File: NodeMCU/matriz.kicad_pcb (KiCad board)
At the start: 2 copper layers, 69 x 68 mm, 25 parts, among them J1 Conn_01x05, Q1 Q_NPN_CBE, Q2 Q_NPN_CBE, Q3 Q_NPN_CBE, SW1 SW_Push_Open, SW2 SW_Push, U3 NodeMCU1.0(ESP-12E)

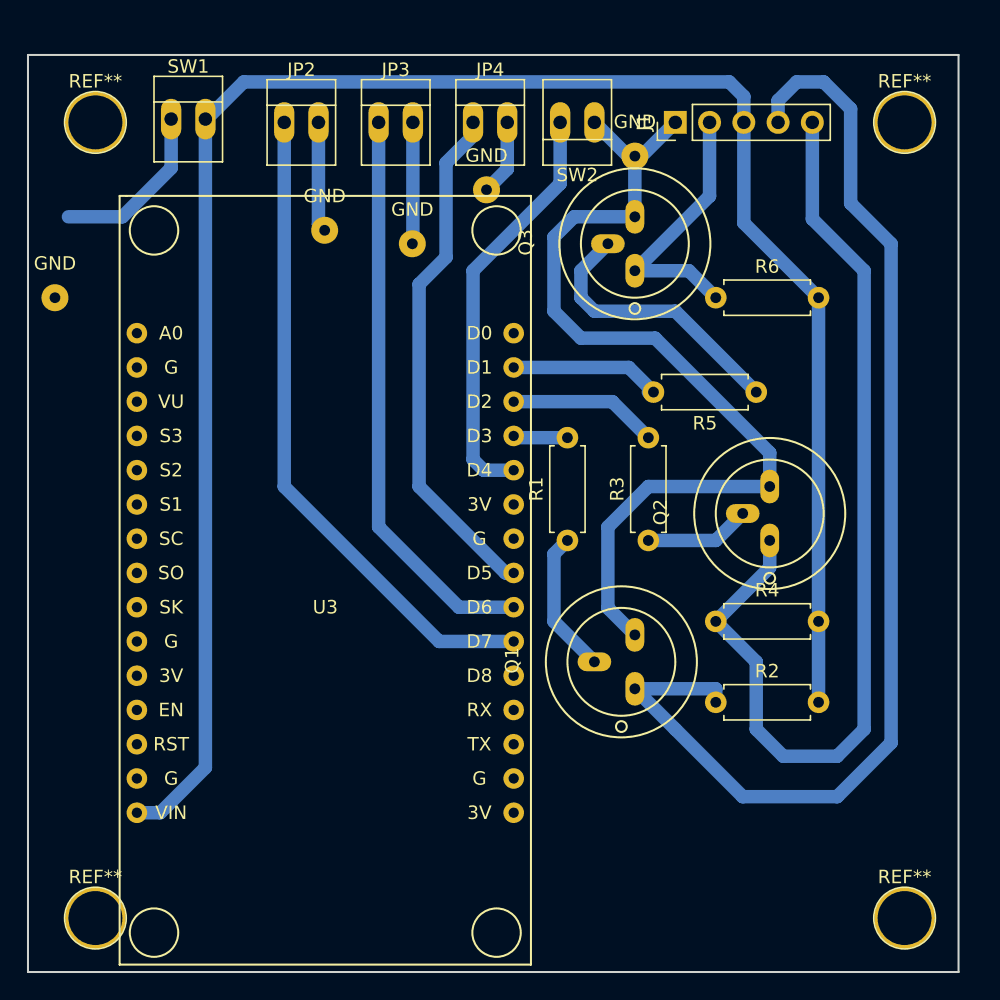
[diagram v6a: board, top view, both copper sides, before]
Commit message: Generacion de pdf final con limites y otras cosas
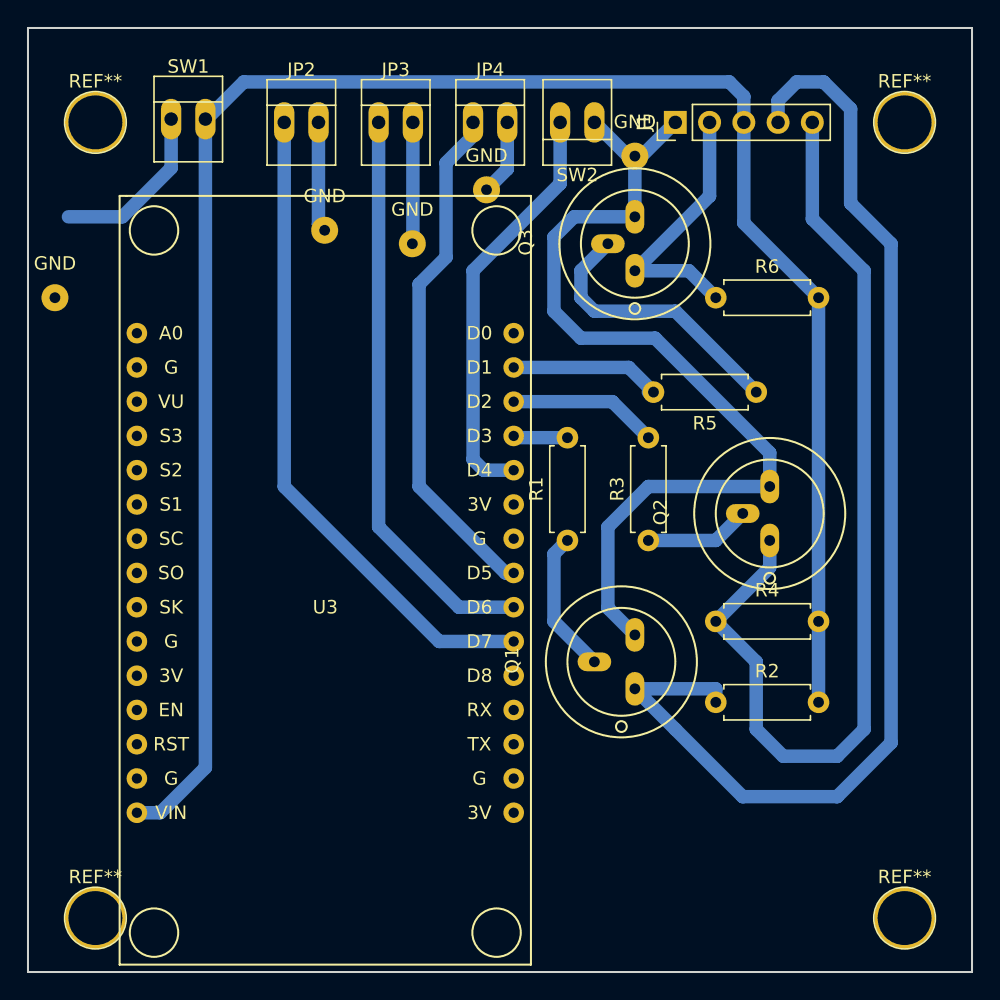
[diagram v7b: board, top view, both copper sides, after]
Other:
- board size 69 x 68 mm -> 70 x 70 mm
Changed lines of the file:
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@@
     (links 32)
     (no_connects 3)
-    (area 83.924999 66.88 164.85 141.700001)
+    (area 83.924999 64.924999 167.35 141.200001)
     (thickness 1.6)
-    (drawings 6)
+    (drawings 8)
     (tracks 98)
     (zones 0)
@@
       (layerselection 0x00000_80000000)
       (usegerberextensions false)
-      (excludeedgelayer true)
+      (excludeedgelayer false)
       (linewidth 1.000000)
       (plotframeref false)
@@
       (drillshape 0)
       (scaleselection 1)
-      (outputdirectory C:/Users/nahuel/git/conexiones/))
+      (outputdirectory C:/Users/nahuel/git/conexiones/NodeMCU/))
   )
   (net 0 "")
@@
     (pad 1 thru_hole circle (at 0 0) (size 1.99898 1.99898) (drill 0.8001) (layers *.Cu *.Mask))
   )
-  (dimension 69 (width 0.3) (layer Dwgs.User)
-    (gr_text "69.000 mm" (at 118.5 140.35) (layer Dwgs.User)
+  (dimension 70 (width 0.3) (layer Dwgs.User)
+    (gr_text "70.000 mm" (at 160.85 100 90) (layer Dwgs.User)
       (effects (font (size 1.5 1.5) (thickness 0.3)))
     )
-    (feature1 (pts (xy 84 135) (xy 84 141.7)))
-    (feature2 (pts (xy 153 135) (xy 153 141.7)))
-    (crossbar (pts (xy 153 139) (xy 84 139)))
-    (arrow1a (pts (xy 84 139) (xy 85.126504 138.413579)))
-    (arrow1b (pts (xy 84 139) (xy 85.126504 139.586421)))
-    (arrow2a (pts (xy 153 139) (xy 151.873496 138.413579)))
-    (arrow2b (pts (xy 153 139) (xy 151.873496 139.586421)))
-  )
-  (dimension 68 (width 0.3) (layer Dwgs.User)
-    (gr_text "68.000 mm" (at 158.35 101 270) (layer Dwgs.User)
+    (feature1 (pts (xy 154 65) (xy 162.2 65)))
+    (feature2 (pts (xy 154 135) (xy 162.2 135)))
+    (crossbar (pts (xy 159.5 135) (xy 159.5 65)))
+    (arrow1a (pts (xy 159.5 65) (xy 160.086421 66.126504)))
+    (arrow1b (pts (xy 159.5 65) (xy 158.913579 66.126504)))
+    (arrow2a (pts (xy 159.5 135) (xy 160.086421 133.873496)))
+    (arrow2b (pts (xy 159.5 135) (xy 158.913579 133.873496)))
+  )
+  (gr_line (start 154 67) (end 154 65) (angle 90) (layer Edge.Cuts) (width 0.15))
+  (gr_line (start 84 65) (end 84 67) (angle 90) (layer Edge.Cuts) (width 0.15))
+  (gr_line (start 154 65) (end 84 65) (angle 90) (layer Edge.Cuts) (width 0.15))
+  (gr_line (start 154 135) (end 154 67) (angle 90) (layer Edge.Cuts) (width 0.15))
+  (gr_line (start 84 135) (end 154 135) (angle 90) (layer Edge.Cuts) (width 0.15))
+  (dimension 70 (width 0.3) (layer Dwgs.User)
+    (gr_text "70.000 mm" (at 119 139.85) (layer Dwgs.User)
       (effects (font (size 1.5 1.5) (thickness 0.3)))
     )
-    (feature1 (pts (xy 153 135) (xy 159.7 135)))
-    (feature2 (pts (xy 153 67) (xy 159.7 67)))
-    (crossbar (pts (xy 157 67) (xy 157 135)))
-    (arrow1a (pts (xy 157 135) (xy 156.413579 133.873496)))
-    (arrow1b (pts (xy 157 135) (xy 157.586421 133.873496)))
-    (arrow2a (pts (xy 157 67) (xy 156.413579 68.126504)))
-    (arrow2b (pts (xy 157 67) (xy 157.586421 68.126504)))
+    (feature1 (pts (xy 154 135) (xy 154 141.2)))
+    (feature2 (pts (xy 84 135) (xy 84 141.2)))
+    (crossbar (pts (xy 84 138.5) (xy 154 138.5)))
+    (arrow1a (pts (xy 154 138.5) (xy 152.873496 139.086421)))
+    (arrow1b (pts (xy 154 138.5) (xy 152.873496 137.913579)))
+    (arrow2a (pts (xy 84 138.5) (xy 85.126504 139.086421)))
+    (arrow2b (pts (xy 84 138.5) (xy 85.126504 137.913579)))
   )
   (gr_line (start 84 135) (end 84 67) (angle 90) (layer Edge.Cuts) (width 0.15))
-  (gr_line (start 153 135) (end 84 135) (angle 90) (layer Edge.Cuts) (width 0.15))
-  (gr_line (start 153 67) (end 153 135) (angle 90) (layer Edge.Cuts) (width 0.15))
-  (gr_line (start 84 67) (end 153 67) (angle 90) (layer Edge.Cuts) (width 0.15))
   (segment (start 105.54 72) (end 105.54 79.54) (width 1) (layer B.Cu) (net 1))
   (segment (start 105.54 79.54) (end 106 80) (width 1) (layer B.Cu) (net 1))

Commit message: Ultimos cambios
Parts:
- added J2: Conn_01x02, Pin_Headers:Pin_Header_Straight_1x02_Pitch2.54mm, F.Cu at (92.0, 81.0)
- U3: footprint ESP8266:NodeMCU1.0(12-E) -> lib:NodeMCU1.0(12-E)
- moved GND 6.32 mm to (92.0, 87.0)
- moved SW1 2.40 mm to (97.0, 72.0)
- moved U3 2.22 mm to (108.0, 109.0)
- moved REF** 2.00 mm to (91.0, 131.0)
- moved REF** 2.00 mm to (91.0, 72.0)
- moved R1 1.00 mm to (124.0, 104.0)
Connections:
- GND pad 1: (no net) -> /GND
- GND pad 1: GNDPWR -> /GND (x4)
- J1 pad 1: GNDPWR -> /GND
- JP2 pad 2: GNDPWR -> /GND
- JP3 pad 2: GNDPWR -> /GND
- JP4 pad 2: GNDPWR -> /GND
- Q1 pad 3: GNDPWR -> /GND
- Q2 pad 3: GNDPWR -> /GND
- Q3 pad 3: GNDPWR -> /GND
- SW1 pad 1: +5V -> /PWR
- SW2 pad 1: GNDPWR -> /GND
- U3 pad 10: Net-(U3-Pad10) -> /GND
- U3 pad 14: Net-(U3-Pad14) -> /GND
- U3 pad 17: Net-(U3-Pad17) -> /GND
- U3 pad 24: Net-(U3-Pad24) -> /GND
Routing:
- net /GND: track 0.00 -> 199.2 mm
- net GNDPWR: track 93.5 -> 0.00 mm
- net +5V: track 12.7 -> 0.00 mm
- net /PWR: track 0.00 -> 9.92 mm
- net Net-(Q1-Pad2): track 10.7 -> 8.83 mm
- net /V+: track 143.3 -> 141.9 mm
- net Net-(JP4-Pad1): track 38.3 -> 39.3 mm
- net Net-(R1-Pad2): track 4.04 -> 4.60 mm
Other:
- board size 70 x 70 mm -> 68 x 68 mm
